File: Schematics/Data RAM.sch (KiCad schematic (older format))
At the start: 9 parts

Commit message: annotate
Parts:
- gave numbers to parts that had none: 9
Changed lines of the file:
@@
 $EndDescr
 $Comp
-L Memory_RAM:IDT71256SA12TPG U?
+L Memory_RAM:IDT71256SA12TPG U12
 U 1 1 5E1E9FA0
 P 6850 2700
-F 0 "U?" H 6400 3650 50  0000 C CNN
+F 0 "U12" H 6400 3650 50  0000 C CNN
 F 1 "IDT71256SA12TPG" H 6400 3550 50  0000 C CNN
 F 2 "" H 6850 4700 50  0001 C CNN
@@
 $EndComp
 $Comp
-L Memory_RAM:IDT71256SA12TPG U?
+L Memory_RAM:IDT71256SA12TPG U13
 U 1 1 5E1EC273
 P 6850 5000
-F 0 "U?" H 6400 5950 50  0000 C CNN
+F 0 "U13" H 6400 5950 50  0000 C CNN
 F 1 "IDT71256SA12TPG" H 6400 5850 50  0000 C CNN
 F 2 "" H 6850 7000 50  0001 C CNN
@@
 $EndComp
 $Comp
-L power:GND #PWR?
+L power:GND #PWR0116
 U 1 1 5E1EE0BF
 P 6850 3650
-F 0 "#PWR?" H 6850 3400 50  0001 C CNN
+F 0 "#PWR0116" H 6850 3400 50  0001 C CNN
 F 1 "GND" H 6855 3477 50  0000 C CNN
 F 2 "" H 6850 3650 50  0001 C CNN
@@
 $EndComp
 $Comp
-L power:GND #PWR?
+L power:GND #PWR0117
 U 1 1 5E1EE650
 P 6850 5950
-F 0 "#PWR?" H 6850 5700 50  0001 C CNN
+F 0 "#PWR0117" H 6850 5700 50  0001 C CNN
 F 1 "GND" H 6855 5777 50  0000 C CNN
 F 2 "" H 6850 5950 50  0001 C CNN
@@
 $EndComp
 $Comp
-L power:VCC #PWR?
+L power:VCC #PWR0118
 U 1 1 5E1EEC64
 P 6850 4150
-F 0 "#PWR?" H 6850 4000 50  0001 C CNN
+F 0 "#PWR0118" H 6850 4000 50  0001 C CNN
 F 1 "VCC" H 6867 4323 50  0000 C CNN
 F 2 "" H 6850 4150 50  0001 C CNN
@@
 $EndComp
 $Comp
-L power:VCC #PWR?
+L power:VCC #PWR0119
 U 1 1 5E1EF332
 P 6850 1850
-F 0 "#PWR?" H 6850 1700 50  0001 C CNN
+F 0 "#PWR0119" H 6850 1700 50  0001 C CNN
 F 1 "VCC" H 6867 2023 50  0000 C CNN
 F 2 "" H 6850 1850 50  0001 C CNN
@@
 P 4700 2400
 AR Path="/5D2C0C74/5E2163C3" Ref="U?"  Part="1"
-AR Path="/5D2C1188/5E2163C3" Ref="U?"  Part="1"
-F 0 "U?" H 4700 2725 50  0000 C CNN
+AR Path="/5D2C1188/5E2163C3" Ref="U10"  Part="1"
+F 0 "U10" H 4700 2725 50  0000 C CNN
 F 1 "74LS32" H 4700 2634 50  0000 C CNN
 F 2 "" H 4700 2400 50  0001 C CNN
@@
 P 4700 1800
 AR Path="/5D2C0C74/5E2163CE" Ref="U?"  Part="1"
-AR Path="/5D2C1188/5E2163CE" Ref="U?"  Part="1"
-F 0 "U?" H 4700 2125 50  0000 C CNN
+AR Path="/5D2C1188/5E2163CE" Ref="U9"  Part="1"
+F 0 "U9" H 4700 2125 50  0000 C CNN
 F 1 "74LS32" H 4700 2034 50  0000 C CNN
 F 2 "" H 4700 1800 50  0001 C CNN
@@
 Connection ~ 5600 2400
 $Comp
-L 74xx:74LS04 U?
+L 74xx:74LS04 U11
 U 1 1 5E2339CC
 P 4750 4550
-F 0 "U?" H 4750 4867 50  0000 C CNN
+F 0 "U11" H 4750 4867 50  0000 C CNN
 F 1 "74LS04" H 4750 4776 50  0000 C CNN
 F 2 "" H 4750 4550 50  0001 C CNN
@@
 P 800 7600
 AR Path="/5D2C07CD/5E262247" Ref="C?"  Part="1"
-AR Path="/5D2C1188/5E262247" Ref="C?"  Part="1"
-F 0 "C?" H 915 7646 50  0000 L CNN
+AR Path="/5D2C1188/5E262247" Ref="C7"  Part="1"
+F 0 "C7" H 915 7646 50  0000 L CNN
 F 1 "100nF" H 915 7555 50  0000 L CNN
 F 2 "" H 838 7450 50  0001 C CNN
@@
 P 1300 7600
 AR Path="/5D2C07CD/5E26224D" Ref="C?"  Part="1"
-AR Path="/5D2C1188/5E26224D" Ref="C?"  Part="1"
-F 0 "C?" H 1415 7646 50  0000 L CNN
+AR Path="/5D2C1188/5E26224D" Ref="C8"  Part="1"
+F 0 "C8" H 1415 7646 50  0000 L CNN
 F 1 "100nF" H 1415 7555 50  0000 L CNN
 F 2 "" H 1338 7450 50  0001 C CNN
@@
 P 1800 7600
 AR Path="/5D2C07CD/5E262253" Ref="C?"  Part="1"
-AR Path="/5D2C1188/5E262253" Ref="C?"  Part="1"
-F 0 "C?" H 1915 7646 50  0000 L CNN
+AR Path="/5D2C1188/5E262253" Ref="C9"  Part="1"
+F 0 "C9" H 1915 7646 50  0000 L CNN
 F 1 "100nF" H 1915 7555 50  0000 L CNN
 F 2 "" H 1838 7450 50  0001 C CNN
@@
 P 2300 7600
 AR Path="/5D2C07CD/5E262259" Ref="C?"  Part="1"
-AR Path="/5D2C1188/5E262259" Ref="C?"  Part="1"
-F 0 "C?" H 2415 7646 50  0000 L CNN
+AR Path="/5D2C1188/5E262259" Ref="C10"  Part="1"
+F 0 "C10" H 2415 7646 50  0000 L CNN
 F 1 "100nF" H 2415 7555 50  0000 L CNN
 F 2 "" H 2338 7450 50  0001 C CNN
@@
 P 800 7750
 AR Path="/5D2C07CD/5E26225F" Ref="#PWR?"  Part="1"
-AR Path="/5D2C1188/5E26225F" Ref="#PWR?"  Part="1"
-F 0 "#PWR?" H 800 7500 50  0001 C CNN
+AR Path="/5D2C1188/5E26225F" Ref="#PWR0120"  Part="1"
+F 0 "#PWR0120" H 800 7500 50  0001 C CNN
 F 1 "GND" H 805 7577 50  0000 C CNN
 F 2 "" H 800 7750 50  0001 C CNN
@@
 P 800 7450
 AR Path="/5D2C07CD/5E262265" Ref="#PWR?"  Part="1"
-AR Path="/5D2C1188/5E262265" Ref="#PWR?"  Part="1"
-F 0 "#PWR?" H 800 7300 50  0001 C CNN
+AR Path="/5D2C1188/5E262265" Ref="#PWR0121"  Part="1"
+F 0 "#PWR0121" H 800 7300 50  0001 C CNN
 F 1 "VCC" H 817 7623 50  0000 C CNN
 F 2 "" H 800 7450 50  0001 C CNN

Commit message: Add footprints to all decoupling caps
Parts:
- C10, C7, C8, C9: footprint (none) -> Capacitor_THT:C_Disc_D4.3mm_W1.9mm_P5.00mm
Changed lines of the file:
@@
 F 0 "C7" H 915 7646 50  0000 L CNN
 F 1 "100nF" H 915 7555 50  0000 L CNN
-F 2 "" H 838 7450 50  0001 C CNN
+F 2 "Capacitor_THT:C_Disc_D4.3mm_W1.9mm_P5.00mm" H 838 7450 50  0001 C CNN
 F 3 "~" H 800 7600 50  0001 C CNN
 	1    800  7600
@@
 F 0 "C8" H 1415 7646 50  0000 L CNN
 F 1 "100nF" H 1415 7555 50  0000 L CNN
-F 2 "" H 1338 7450 50  0001 C CNN
+F 2 "Capacitor_THT:C_Disc_D4.3mm_W1.9mm_P5.00mm" H 1338 7450 50  0001 C CNN
 F 3 "~" H 1300 7600 50  0001 C CNN
 	1    1300 7600
@@
 F 0 "C9" H 1915 7646 50  0000 L CNN
 F 1 "100nF" H 1915 7555 50  0000 L CNN
-F 2 "" H 1838 7450 50  0001 C CNN
+F 2 "Capacitor_THT:C_Disc_D4.3mm_W1.9mm_P5.00mm" H 1838 7450 50  0001 C CNN
 F 3 "~" H 1800 7600 50  0001 C CNN
 	1    1800 7600
@@
 F 0 "C10" H 2415 7646 50  0000 L CNN
 F 1 "100nF" H 2415 7555 50  0000 L CNN
-F 2 "" H 2338 7450 50  0001 C CNN
+F 2 "Capacitor_THT:C_Disc_D4.3mm_W1.9mm_P5.00mm" H 2338 7450 50  0001 C CNN
 F 3 "~" H 2300 7600 50  0001 C CNN
 	1    2300 7600

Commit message: Assign a bunch more footprints. All are assigned now.
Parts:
- U10, U11, U9: footprint (none) -> Package_DIP:DIP-14_W7.62mm
- U12, U13: footprint (none) -> Package_DIP:DIP-28_W7.62mm_Socket
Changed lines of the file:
@@
 F 0 "U12" H 6400 3650 50  0000 C CNN
 F 1 "IDT71256SA12TPG" H 6400 3550 50  0000 C CNN
-F 2 "" H 6850 4700 50  0001 C CNN
+F 2 "Package_DIP:DIP-28_W7.62mm_Socket" H 6850 4700 50  0001 C CNN
 F 3 "" H 6850 4700 50  0001 C CNN
 	1    6850 2700
@@
 F 0 "U13" H 6400 5950 50  0000 C CNN
 F 1 "IDT71256SA12TPG" H 6400 5850 50  0000 C CNN
-F 2 "" H 6850 7000 50  0001 C CNN
+F 2 "Package_DIP:DIP-28_W7.62mm_Socket" H 6850 7000 50  0001 C CNN
 F 3 "" H 6850 7000 50  0001 C CNN
 	1    6850 5000
@@
 F 0 "U10" H 4700 2725 50  0000 C CNN
 F 1 "74LS32" H 4700 2634 50  0000 C CNN
-F 2 "" H 4700 2400 50  0001 C CNN
+F 2 "Package_DIP:DIP-14_W7.62mm" H 4700 2400 50  0001 C CNN
 F 3 "http://www.ti.com/lit/gpn/sn74LS32" H 4700 2400 50  0001 C CNN
 	1    4700 2400
@@
 F 0 "U9" H 4700 2125 50  0000 C CNN
 F 1 "74LS32" H 4700 2034 50  0000 C CNN
-F 2 "" H 4700 1800 50  0001 C CNN
+F 2 "Package_DIP:DIP-14_W7.62mm" H 4700 1800 50  0001 C CNN
 F 3 "http://www.ti.com/lit/gpn/sn74LS32" H 4700 1800 50  0001 C CNN
 	1    4700 1800
@@
 F 0 "U11" H 4750 4867 50  0000 C CNN
 F 1 "74LS04" H 4750 4776 50  0000 C CNN
-F 2 "" H 4750 4550 50  0001 C CNN
+F 2 "Package_DIP:DIP-14_W7.62mm" H 4750 4550 50  0001 C CNN
 F 3 "http://www.ti.com/lit/gpn/sn74LS04" H 4750 4550 50  0001 C CNN
 	1    4750 4550

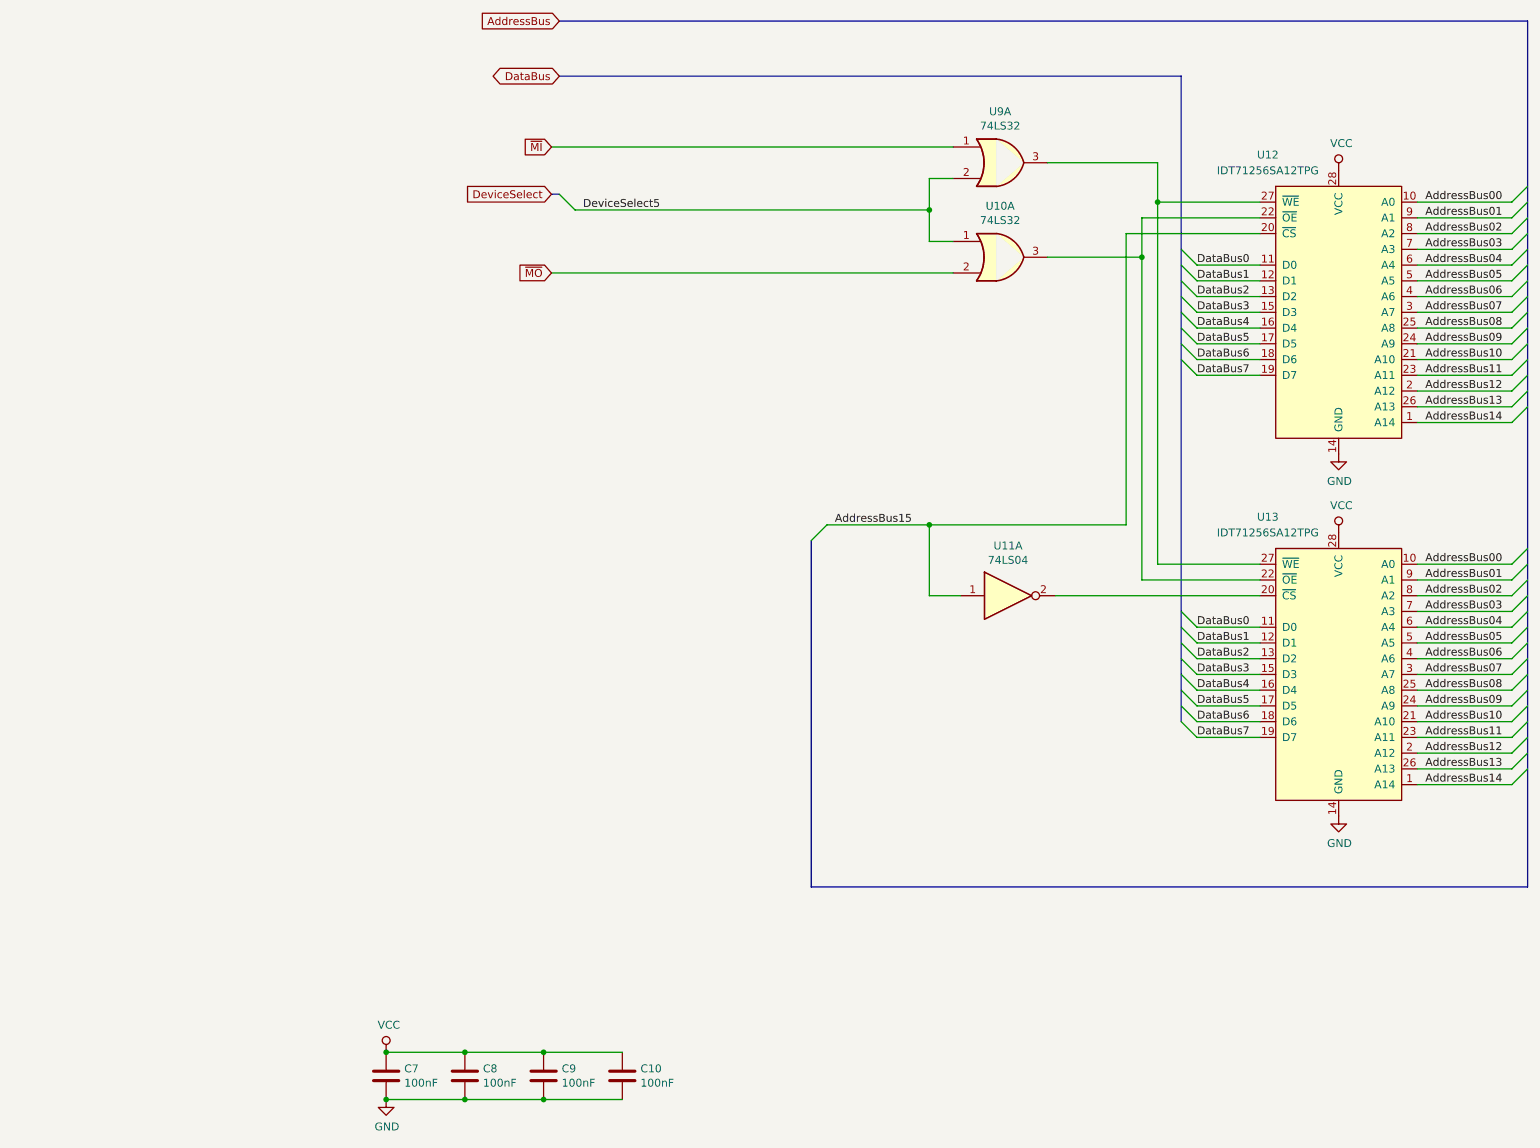
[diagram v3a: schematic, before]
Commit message: My buses were not named according the rules in the Eeschema manual.
Buses which connect to global labels must be named specially.
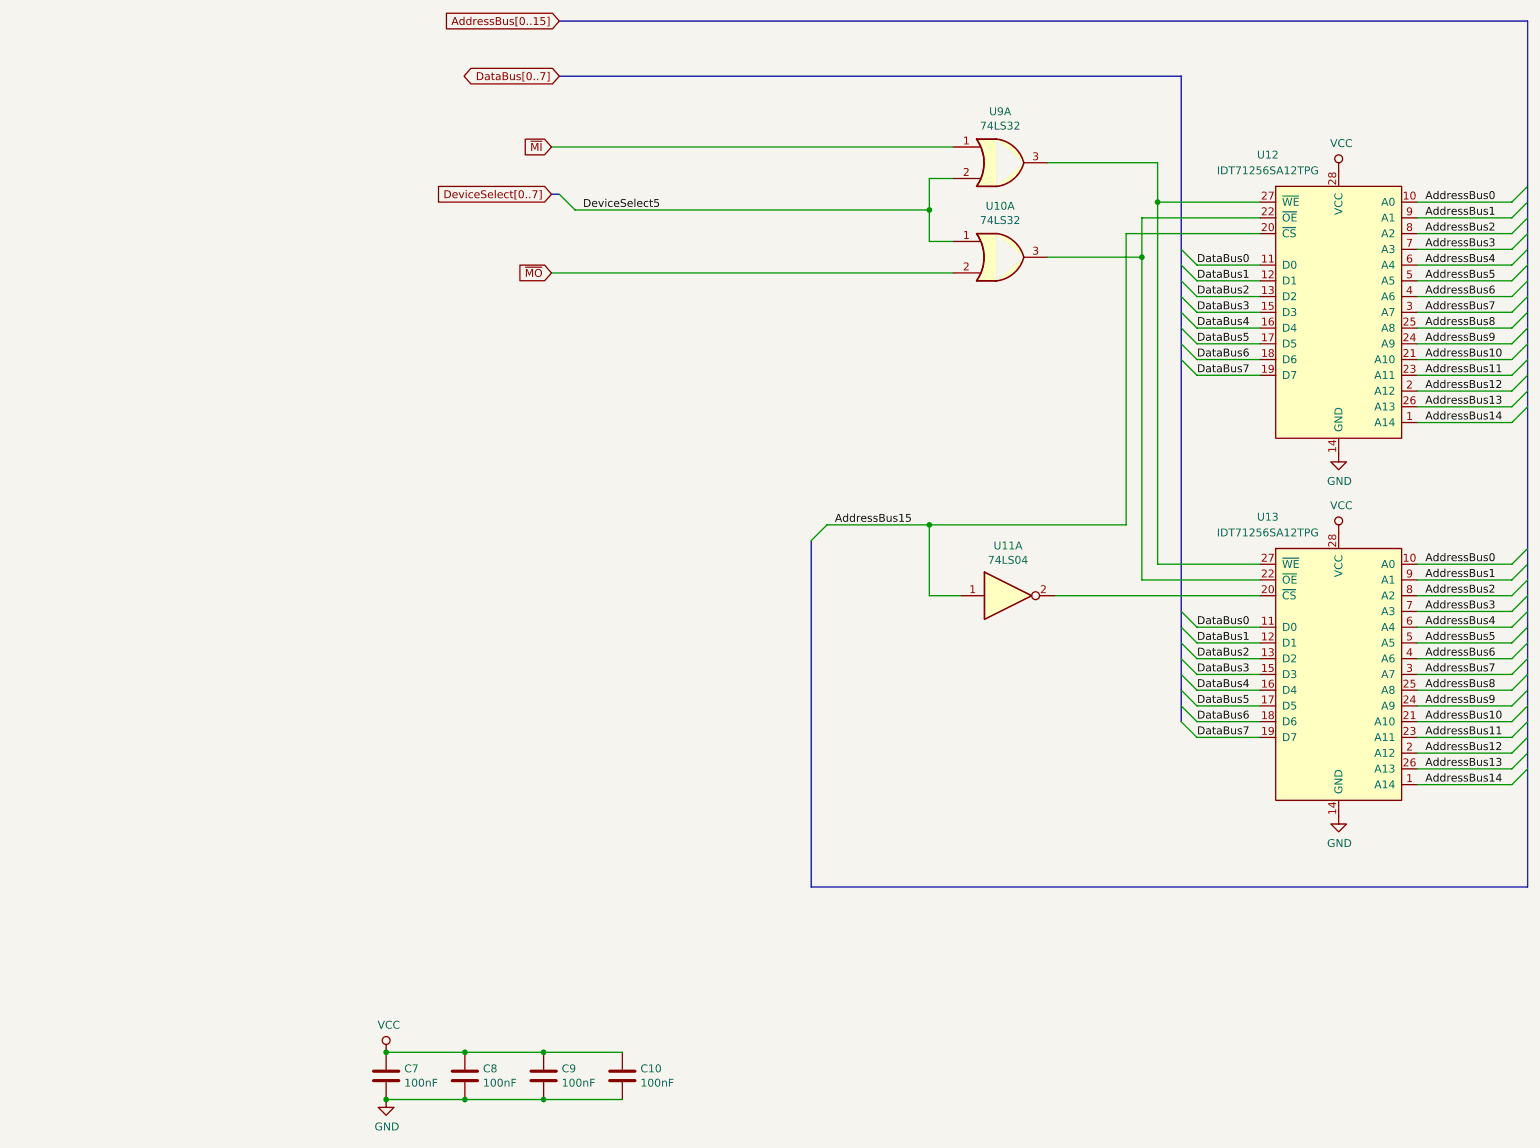
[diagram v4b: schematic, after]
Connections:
- net AddressBus00 renamed AddressBus0
- net AddressBus01 renamed AddressBus1
- net AddressBus02 renamed AddressBus2
- net AddressBus03 renamed AddressBus3
- net AddressBus04 renamed AddressBus4
- net AddressBus05 renamed AddressBus5
- net AddressBus06 renamed AddressBus6
- net AddressBus07 renamed AddressBus7
- net AddressBus08 renamed AddressBus8
- net AddressBus09 renamed AddressBus9
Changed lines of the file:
@@
 	7350 3450 7950 3450
 Text Label 7400 2050 0    50   ~ 0
-AddressBus00
+AddressBus0
 Wire Wire Line
 	7950 2850 7350 2850
@@
 	7950 2050 8050 1950
 Text Label 7400 2150 0    50   ~ 0
-AddressBus01
+AddressBus1
 Text Label 7400 2250 0    50   ~ 0
-AddressBus02
+AddressBus2
 Text Label 7400 2350 0    50   ~ 0
-AddressBus03
+AddressBus3
 Text Label 7400 2450 0    50   ~ 0
-AddressBus04
+AddressBus4
 Text Label 7400 2550 0    50   ~ 0
-AddressBus05
+AddressBus5
 Text Label 7400 2650 0    50   ~ 0
-AddressBus06
+AddressBus6
 Text Label 7400 2750 0    50   ~ 0
-AddressBus07
+AddressBus7
 Text Label 7400 2850 0    50   ~ 0
-AddressBus08
+AddressBus8
 Text Label 7400 2950 0    50   ~ 0
-AddressBus09
+AddressBus9
 Text Label 7400 3050 0    50   ~ 0
 AddressBus10
@@
 	7350 5750 7950 5750
 Text Label 7400 4350 0    50   ~ 0
-AddressBus00
+AddressBus0
 Wire Wire Line
 	7950 5150 7350 5150
@@
 	7950 4350 8050 4250
 Text Label 7400 4450 0    50   ~ 0
-AddressBus01
+AddressBus1
 Text Label 7400 4550 0    50   ~ 0
-AddressBus02
+AddressBus2
 Text Label 7400 4650 0    50   ~ 0
-AddressBus03
+AddressBus3
 Text Label 7400 4750 0    50   ~ 0
-AddressBus04
+AddressBus4
 Text Label 7400 4850 0    50   ~ 0
-AddressBus05
+AddressBus5
 Text Label 7400 4950 0    50   ~ 0
-AddressBus06
+AddressBus6
 Text Label 7400 5050 0    50   ~ 0
-AddressBus07
+AddressBus7
 Text Label 7400 5150 0    50   ~ 0
-AddressBus08
+AddressBus8
 Text Label 7400 5250 0    50   ~ 0
-AddressBus09
+AddressBus9
 Text Label 7400 5350 0    50   ~ 0
 AddressBus10
@@
 AddressBus14
 Text GLabel 1900 900  0    50   Input ~ 0
-AddressBus
+AddressBus[0..15]
 Wire Bus Line
 	8050 900  1900 900
@@
 DataBus7
 Text GLabel 1900 1250 0    50   BiDi ~ 0
-DataBus
+DataBus[0..7]
 Wire Bus Line
 	5850 1250 1900 1250
 Text GLabel 1850 2000 0    50   Input ~ 0
-DeviceSelect
+DeviceSelect[0..7]
 Text GLabel 1850 1700 0    50   Input ~ 0
 ~MI
